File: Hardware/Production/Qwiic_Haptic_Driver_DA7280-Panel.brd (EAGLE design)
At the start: 123.2 x 117.3 mm, 758 parts, among them J1 QWIIC_RIGHT_ANGLE, J10 QWIIC_RIGHT_ANGLE, J13 QWIIC_RIGHT_ANGLE, J14 QWIIC_RIGHT_ANGLE, J17 QWIIC_RIGHT_ANGLE, J18 QWIIC_RIGHT_ANGLE, J2 QWIIC_RIGHT_ANGLE, J21 QWIIC_RIGHT_ANGLE, J22 QWIIC_RIGHT_ANGLE, J25 QWIIC_RIGHT_ANGLE, J26 QWIIC_RIGHT_ANGLE, J29 QWIIC_RIGHT_ANGLE, J30 QWIIC_RIGHT_ANGLE, J33 QWIIC_RIGHT_ANGLE, J34 QWIIC_RIGHT_ANGLE, J37 QWIIC_RIGHT_ANGLE, J38 QWIIC_RIGHT_ANGLE, J41 QWIIC_RIGHT_ANGLE, J42 QWIIC_RIGHT_ANGLE, J45 QWIIC_RIGHT_ANGLE, J46 QWIIC_RIGHT_ANGLE, J49 QWIIC_RIGHT_ANGLE, J5 QWIIC_RIGHT_ANGLE, J50 QWIIC_RIGHT_ANGLE, J53 QWIIC_RIGHT_ANGLE, J54 QWIIC_RIGHT_ANGLE, J57 QWIIC_RIGHT_ANGLE, J58 QWIIC_RIGHT_ANGLE, J6 QWIIC_RIGHT_ANGLE, J61 QWIIC_RIGHT_ANGLE, J62 QWIIC_RIGHT_ANGLE, J9 QWIIC_RIGHT_ANGLE, M1 G1040003D_LRA_CASTELLATED, M10 G1040003D_LRA_CASTELLATED, M11 G1040003D_LRA_CASTELLATED, M12 G1040003D_LRA_CASTELLATED, M13 G1040003D_LRA_CASTELLATED, M14 G1040003D_LRA_CASTELLATED, M15 G1040003D_LRA_CASTELLATED, M16 G1040003D_LRA_CASTELLATED, M2 G1040003D_LRA_CASTELLATED, M3 G1040003D_LRA_CASTELLATED, M4 G1040003D_LRA_CASTELLATED, M5 G1040003D_LRA_CASTELLATED, M6 G1040003D_LRA_CASTELLATED, M7 G1040003D_LRA_CASTELLATED, M8 G1040003D_LRA_CASTELLATED, M9 G1040003D_LRA_CASTELLATED, U1 HAPTIC_DRIVER_DA7280, U10 HAPTIC_DRIVER_DA7280, U11 HAPTIC_DRIVER_DA7280, U12 HAPTIC_DRIVER_DA7280, U13 HAPTIC_DRIVER_DA7280, U14 HAPTIC_DRIVER_DA7280, U15 HAPTIC_DRIVER_DA7280, U16 HAPTIC_DRIVER_DA7280, U2 HAPTIC_DRIVER_DA7280, U3 HAPTIC_DRIVER_DA7280, U4 HAPTIC_DRIVER_DA7280, U5 HAPTIC_DRIVER_DA7280, U6 HAPTIC_DRIVER_DA7280, U7 HAPTIC_DRIVER_DA7280, U8 HAPTIC_DRIVER_DA7280, U9 HAPTIC_DRIVER_DA7280

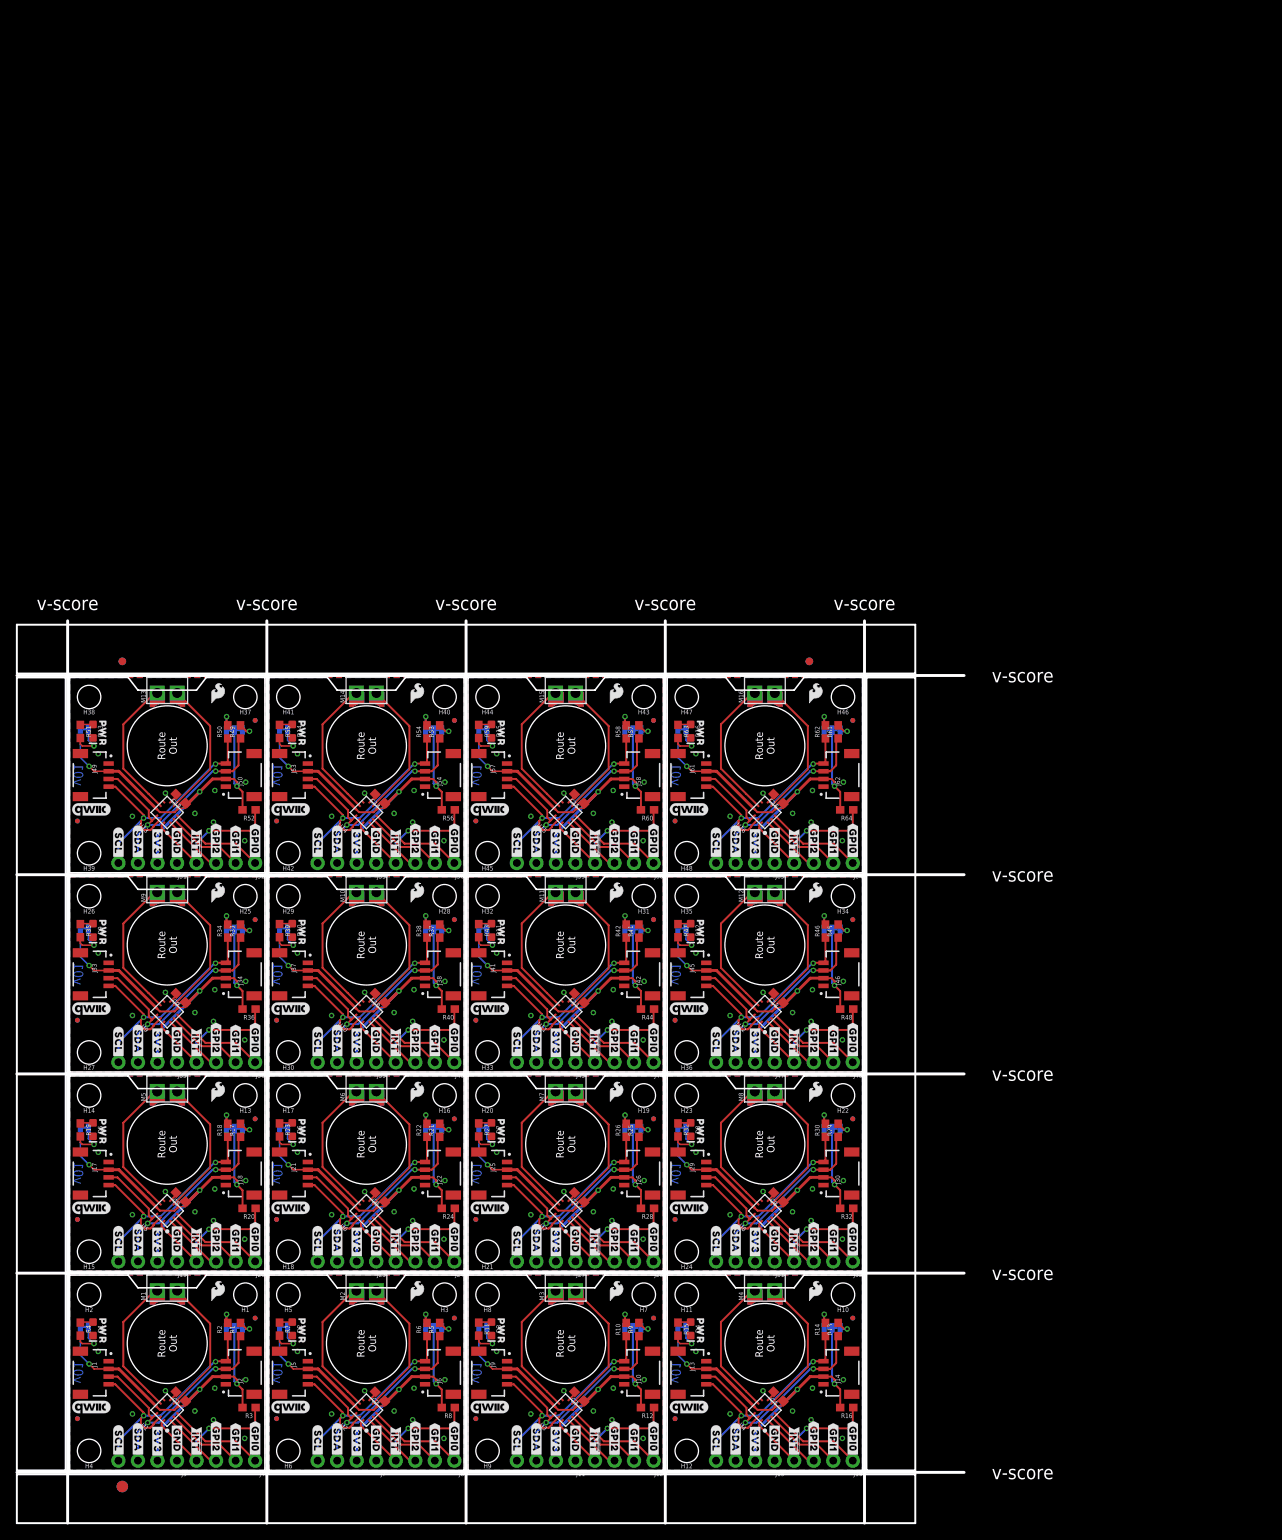
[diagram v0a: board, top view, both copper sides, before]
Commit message: Improves ground pour just a smidge, found better routing options when reviewing panel
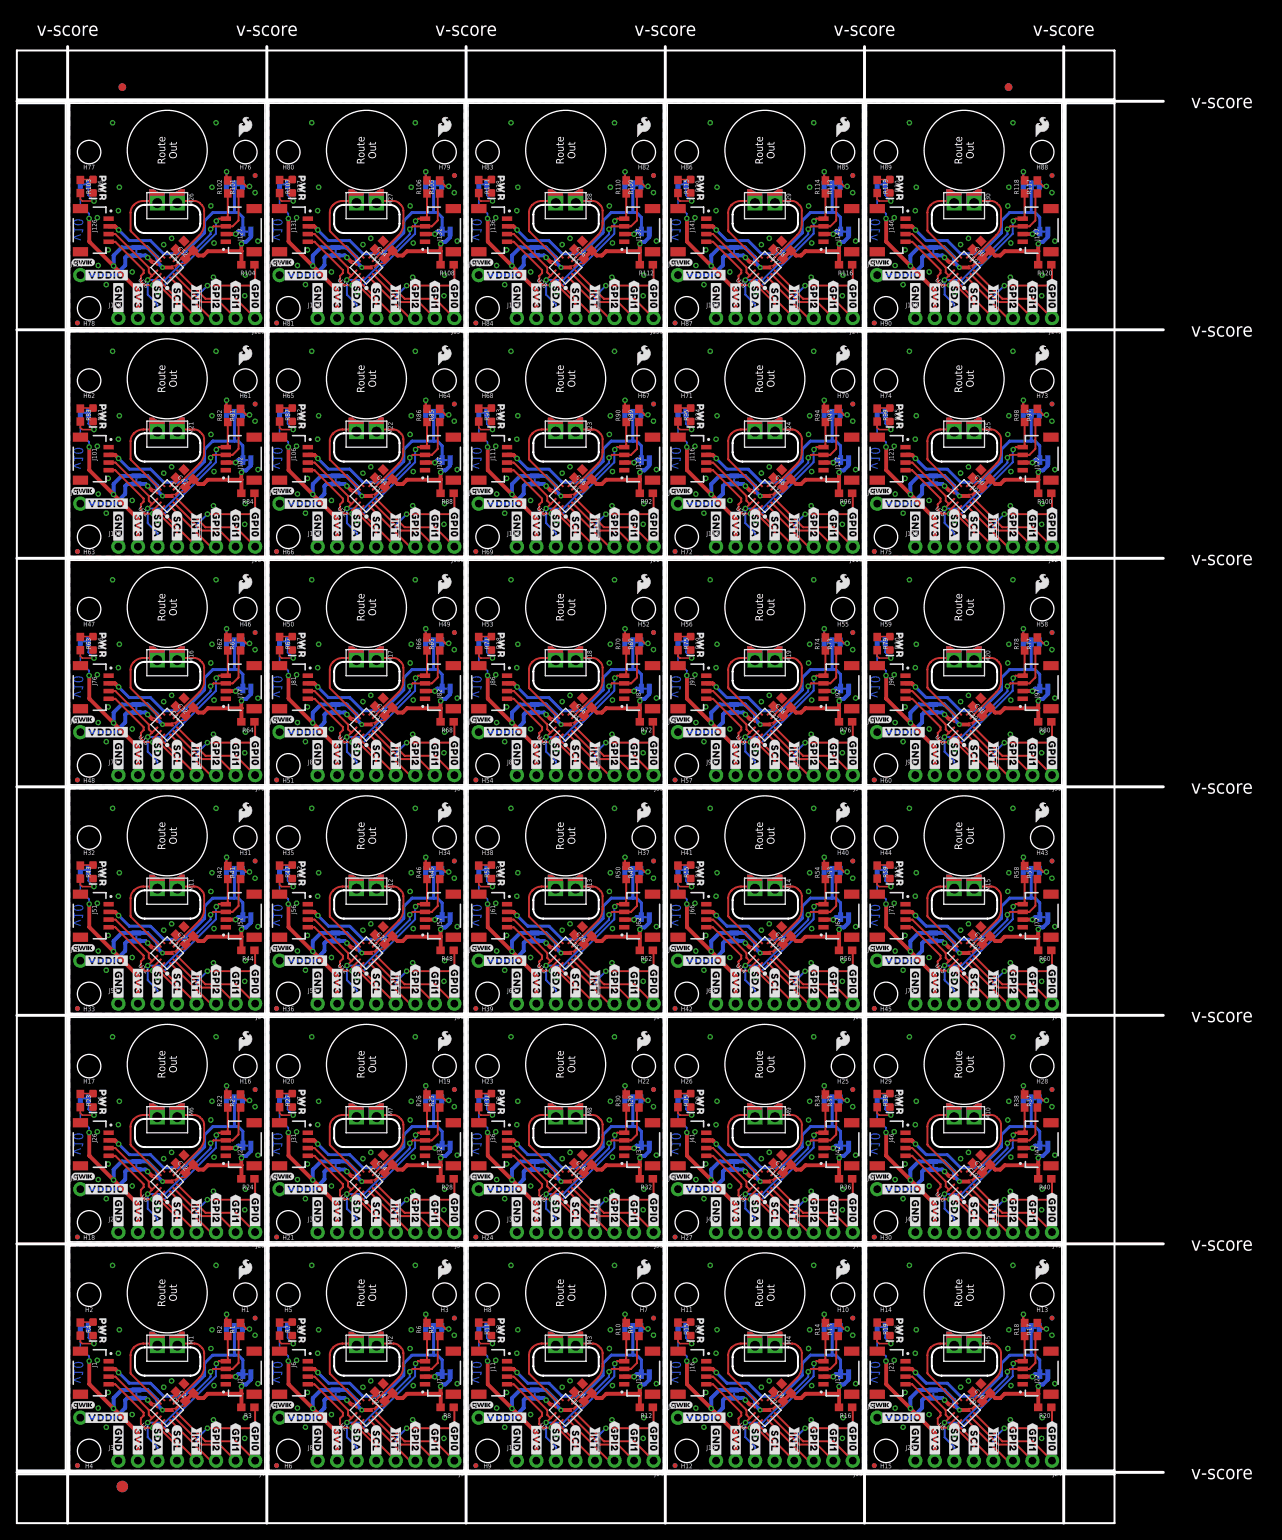
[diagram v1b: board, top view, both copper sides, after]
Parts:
- added C17, C19, C21, C23, C25, C27, C29, C31, C33, C35, C37, C39, C41, C43, C45, C47, C49, C51, C53, C55, C57, C59: 0.1uF, SparkFun-Capacitors:0603
- added C18, C20, C22, C24, C26, C28, C30, C32, C34, C36, C38, C40, C42, C44, C46, C48, C50, C52, C54, C56, C58, C60: 4.7uF, SparkFun-Capacitors:0603
- added D17, D18, D19, D20, D21, D22, D23, D24, D25, D26, D27, D28, D29, D30: RED, SparkFun-LED:LED-0603
- added FD100, FD101, FD102, FD103, FD104, FD105, FD106, FD107, FD108, FD109, FD110, FD111, FD112, FD113, FD114, FD115, FD116, FD117, FD118, FD119, FD120, FD65, FD66, FD67, FD68, FD69, FD70, FD71, FD72, FD73, FD74, FD75, FD76, FD77, FD78, FD79, FD80, FD81, FD82, FD83, FD84, FD85, FD86, FD87, FD88, FD89, FD90, FD91, FD92, FD93, FD94, FD95, FD96, FD97, FD98, FD99: FIDUCIALUFIDUCIAL, SparkFun-Aesthetics:FIDUCIAL-MICRO
- added H49, H50, H51, H52, H53, H54, H55, H56, H57, H58, H59, H60, H61, H62, H63, H64, H65, H66, H67, H68, H69, H70, H71, H72, H73, H74, H75, H76, H77, H78, H79, H80, H81, H82, H83, H84, H85, H86, H87, H88, H89, H90: STAND-OFFTIGHT, SparkFun-Hardware:STAND-OFF-TIGHT
- added J100, J105, J110, J115, J120, J125, J130, J135, J140, J145, J150, J65, J70, J75, J80, J85, J90, J95: (no value), SparkFun-Connectors:1X01_NO_SILK
- added J101, J102, J106, J107, J111, J112, J116, J117, J121, J122, J126, J127, J131, J132, J136, J137, J141, J142, J146, J147, J66, J67, J71, J72, J76, J77, J81, J82, J86, J87, J91, J92, J96, J97: QWIIC_RIGHT_ANGLE, SparkFun-Connectors:JST04_1MM_RA
- added J103, J104, J108, J109, J113, J114, J118, J119, J123, J124, J128, J129, J133, J134, J138, J139, J143, J144, J148, J149, J68, J69, J73, J74, J78, J79, J83, J84, J88, J89, J93, J94, J98, J99: (no value), SparkFun-Connectors:1X04_NO_SILK
- added JP100, JP101, JP103, JP104, JP105, JP107, JP108, JP109, JP111, JP112, JP113, JP115, JP116, JP117, JP119, JP120, JP33, JP35, JP36, JP37, JP39, JP40, JP41, JP43, JP44, JP45, JP47, JP48, JP49, JP51, JP52, JP53, JP55, JP56, JP57, JP59, JP60, JP61, JP63, JP64, JP65, JP67, JP68, JP69, JP71, JP72, JP73, JP75, JP76, JP77, JP79, JP80, JP81, JP83, JP84, JP85, JP87, JP88, JP89, JP91, JP92, JP93, JP95, JP96, JP97, JP99: LED, SparkFun-Jumpers:SMT-JUMPER_2_NC_TRACE_SILK
- added JP102, JP106, JP110, JP114, JP118, JP34, JP38, JP42, JP46, JP50, JP54, JP58, JP62, JP66, JP70, JP74, JP78, JP82, JP86, JP90, JP94, JP98: I2C_PU, SparkFun-Jumpers:SMT-JUMPER_3_2-NC_TRACE_SILK
- added LOGO1, LOGO11, LOGO13, LOGO15, LOGO17, LOGO19, LOGO2, LOGO21, LOGO23, LOGO25, LOGO27, LOGO29, LOGO31, LOGO33, LOGO35, LOGO37, LOGO39, LOGO41, LOGO43, LOGO45, LOGO47, LOGO49, LOGO5, LOGO51, LOGO53, LOGO55, LOGO57, LOGO59, LOGO7, LOGO9: OSHW-LOGOS, SparkFun-Aesthetics:OSHW-LOGO-S
- added LOGO10, LOGO12, LOGO14, LOGO16, LOGO18, LOGO20, LOGO22, LOGO24, LOGO26, LOGO28, LOGO3, LOGO30, LOGO32, LOGO34, LOGO36, LOGO38, LOGO4, LOGO40, LOGO42, LOGO44, LOGO46, LOGO48, LOGO50, LOGO52, LOGO54, LOGO56, LOGO58, LOGO6, LOGO60, LOGO8: SFE_LOGO_FLAME.1_INCH, SparkFun-Aesthetics:SFE_LOGO_FLAME_.1
- added M17, M18, M19, M20, M21, M22, M23, M24, M25, M26, M27, M28, M29, M30: G1040003D_LRA_CASTELLATED, TEMP:COIN_VIBRATION_MOTOR_CASTEL
- added R100, R104, R108, R112, R116, R120, R68, R72, R76, R80, R84, R88, R92, R96: 10k, SparkFun-Resistors:0603
- added R101, R102, R105, R106, R109, R110, R113, R114, R117, R118, R65, R66, R69, R70, R73, R74, R77, R78, R81, R82, R85, R86, R89, R90, R93, R94, R97, R98: 4.7k, SparkFun-Resistors:0603
- added R103, R107, R111, R115, R119, R67, R71, R75, R79, R83, R87, R91, R95, R99: 1k, SparkFun-Resistors:0603
- added U$417, U$437, U$446, U$466, U$475, U$495, U$504, U$524, U$533, U$553, U$562, U$582, U$591, U$611, U$620, U$640, U$649, U$669, U$678, U$698, U$707, U$727, U$736, U$756, U$765, U$785, U$794, U$814, U$823, U$843, U$852: (no value), top:#GND#0
- added U$418, U$447, U$476, U$505, U$534, U$563, U$592, U$621, U$650, U$679, U$708, U$737, U$766, U$795, U$824, U$853: (no value), top:#SCL#5
- added U$419, U$448, U$477, U$506, U$535, U$564, U$593, U$622, U$651, U$680, U$709, U$738, U$767, U$796, U$825, U$854: (no value), top:PWR72810
- added U$420, U$449, U$478, U$507, U$536, U$565, U$594, U$623, U$652, U$681, U$710, U$739, U$768, U$797, U$826, U$855: (no value), bot:#SCL#1
- added U$421, U$450, U$479, U$508, U$537, U$566, U$595, U$624, U$653, U$682, U$711, U$740, U$769, U$798, U$827, U$856: (no value), bot:#I2C#4
- added U$422, U$451, U$480, U$509, U$538, U$567, U$596, U$625, U$654, U$683, U$712, U$741, U$770, U$799, U$828, U$857: (no value), bot:#LED#4
- added U$423, U$452, U$481, U$510, U$539, U$568, U$597, U$626, U$655, U$684, U$713, U$742, U$771, U$800, U$829, U$858: (no value), top:#3V3#1
- added U$424, U$453, U$482, U$511, U$540, U$569, U$598, U$627, U$656, U$685, U$714, U$743, U$772, U$801, U$830, U$859: (no value), SparkFun-Aesthetics:SFE_LOGO_FLAME_.1
- added U$425, U$454, U$483, U$512, U$541, U$570, U$599, U$628, U$657, U$686, U$715, U$744, U$773, U$802, U$831, U$860: (no value), bot:##INT##3
- added U$426, U$455, U$484, U$513, U$542, U$571, U$600, U$629, U$658, U$687, U$716, U$745, U$774, U$803, U$832, U$861: (no value), top:##INT##6
- added U$427, U$456, U$485, U$514, U$543, U$572, U$601, U$630, U$659, U$688, U$717, U$746, U$775, U$804, U$833, U$862: (no value), top:#VDD#4
- added U$428, U$429, U$457, U$458, U$486, U$487, U$515, U$516, U$544, U$545, U$573, U$574, U$602, U$603, U$631, U$632, U$660, U$661, U$689, U$690, U$718, U$719, U$747, U$748, U$776, U$777, U$805, U$806, U$834, U$835, U$863, U$864: (no value), top:#VDDIO#5
- added U$430, U$459, U$488, U$517, U$546, U$575, U$604, U$633, U$662, U$691, U$720, U$749, U$778, U$807, U$836, U$865: (no value), top:HAPTIC6
- added U$431, U$460, U$489, U$518, U$547, U$576, U$605, U$634, U$663, U$692, U$721, U$750, U$779, U$808, U$837, U$866: (no value), top:MOTOR7
- added U$432, U$461, U$490, U$519, U$548, U$577, U$606, U$635, U$664, U$693, U$722, U$751, U$780, U$809, U$838, U$867: (no value), top:DRIVER8
- added U$433, U$462, U$491, U$520, U$549, U$578, U$607, U$636, U$665, U$694, U$723, U$752, U$781, U$810, U$839, U$868: (no value), top:DA72809
- added U$434, U$463, U$492, U$521, U$550, U$579, U$608, U$637, U$666, U$695, U$724, U$753, U$782, U$811, U$840, U$869: (no value), top:#IO#6
- added U$435, U$464, U$493, U$522, U$551, U$580, U$609, U$638, U$667, U$696, U$725, U$754, U$783, U$812, U$841, U$870: (no value), bot:#QISO#0
- added U$436, U$465, U$494, U$523, U$552, U$581, U$610, U$639, U$668, U$697, U$726, U$755, U$784, U$813, U$842: QWIIC_LOGO_3MM, SparkFun-Aesthetics:QWIIC_3MM
- added U$438, U$467, U$496, U$525, U$554, U$583, U$612, U$641, U$670, U$699, U$728, U$757, U$786, U$815, U$844: (no value), top:#GPI0#6
- added U$439, U$468, U$497, U$526, U$555, U$584, U$613, U$642, U$671, U$700, U$729, U$758, U$787, U$816, U$845: (no value), top:#GPI1#6
- added U$440, U$469, U$498, U$527, U$556, U$585, U$614, U$643, U$672, U$701, U$730, U$759, U$788, U$817, U$846: (no value), top:#GPI2#6
- added U$441, U$470, U$499, U$528, U$557, U$586, U$615, U$644, U$673, U$702, U$731, U$760, U$789, U$818, U$847: (no value), top:#SDA#4
- added U$442, U$471, U$500, U$529, U$558, U$587, U$616, U$645, U$674, U$703, U$732, U$761, U$790, U$819, U$848: (no value), bot:#GPI0#PWM#2
- added U$443, U$472, U$501, U$530, U$559, U$588, U$617, U$646, U$675, U$704, U$733, U$762, U$791, U$820, U$849: (no value), bot:#GPI1#2
- added U$444, U$473, U$502, U$531, U$560, U$589, U$618, U$647, U$676, U$705, U$734, U$763, U$792, U$821, U$850: (no value), bot:#GPI2#2
- added U$445, U$474, U$503, U$532, U$561, U$590, U$619, U$648, U$677, U$706, U$735, U$764, U$793, U$822, U$851: (no value), bot:#SDA#0
- added U17, U18, U19, U20, U21, U22, U23, U24, U25, U26, U27, U28, U29, U30: HAPTIC_DRIVER_DA7280, TEMP:QFN_DA7280
- C10, C12, C14, C16, C2, C4, C6, C8: value 0.1uF -> 4.7uF
- J10, J25, J30, J45, J5, J50: value QWIIC_RIGHT_ANGLE -> (none); device SparkFun-Connectors:JST04_1MM_RA -> SparkFun-Connectors:1X01_NO_SILK
- J11, J12, J16, J27, J31, J32, J36, J47, J51, J52, J56, J7: value (none) -> QWIIC_RIGHT_ANGLE; device SparkFun-Connectors:1X04_NO_SILK -> SparkFun-Connectors:JST04_1MM_RA
- J13, J14, J18, J29, J33, J34, J38, J49, J53, J54, J58, J9: value QWIIC_RIGHT_ANGLE -> (none); device SparkFun-Connectors:JST04_1MM_RA -> SparkFun-Connectors:1X04_NO_SILK
- J15, J20, J35, J40, J55, J60: device SparkFun-Connectors:1X04_NO_SILK -> SparkFun-Connectors:1X01_NO_SILK
- JP12, JP16, JP20, JP24, JP28, JP32, JP4, JP8: value I2C_PU -> LED; device SparkFun-Jumpers:SMT-JUMPER_3_2-NC_TRACE_SILK -> SparkFun-Jumpers:SMT-JUMPER_2_NC_TRACE_SILK
- U$1: value QWIIC_LOGO_5MM -> QWIIC_LOGO_3MM; device SparkFun-Aesthetics:QWIIC_5MM -> SparkFun-Aesthetics:QWIIC_3MM
- U$10, U$112: device top:HAPTIC7 -> top:MOTOR7
- U$100: device top:#3V3#1 -> top:PWR72810
- U$101, U$362: device SparkFun-Aesthetics:SFE_LOGO_FLAME_.1 -> bot:#SCL#1
- U$102: device SparkFun-Aesthetics:SFE_LOGO_FLAME_.1 -> bot:#I2C#4
- U$103: device bot:##INT##3 -> bot:#LED#4
- U$104: device top:##INT##6 -> top:#3V3#1
- U$105: value QWIIC_LOGO_5MM -> (none); device SparkFun-Aesthetics:QWIIC_5MM -> SparkFun-Aesthetics:SFE_LOGO_FLAME_.1
- U$106, U$222: device top:#GND#0 -> bot:##INT##3
- U$107: device top:#GPI0#6 -> top:##INT##6
- U$108: device top:#GPI1#6 -> top:#VDD#4
- U$109: device top:#GPI2#6 -> top:#VDDIO#5
- U$11, U$113: device top:MOTOR_DRIVER8 -> top:DRIVER8
- U$110, U$370: device top:#SDA#4 -> top:#VDDIO#5
- U$111, U$9: device top:DA72809 -> top:HAPTIC6
- U$114: device bot:#GPI0#PWM#2 -> top:DA72809
- U$115: device bot:#GPI1#2 -> top:#IO#6
- U$116: device bot:#GPI2#2 -> bot:#QISO#0
- U$117: value (none) -> QWIIC_LOGO_3MM; device bot:#SDA#0 -> SparkFun-Aesthetics:QWIIC_3MM
- U$119: device top:#SCL#5 -> top:#GPI0#6
- U$120: device top:PWR72810 -> top:#GPI1#6
- U$121: device bot:#SCL#1 -> top:#GPI2#6
- U$122: device SparkFun-Aesthetics:OSHW-LOGO-MINI -> top:#SDA#4
- U$123: device bot:#I2C#4 -> bot:#GPI0#PWM#2
- U$124: device bot:#LED#4 -> bot:#GPI1#2
- U$125, U$386: device top:#3V3#1 -> bot:#GPI2#2
- U$126: device top:#3V3#1 -> bot:#SDA#0
- U$127, U$205, U$388: device SparkFun-Aesthetics:SFE_LOGO_FLAME_.1 -> top:#GND#0
- U$128: device SparkFun-Aesthetics:SFE_LOGO_FLAME_.1 -> top:#SCL#5
- U$129: device bot:##INT##3 -> top:PWR72810
- U$130: device top:##INT##6 -> bot:#SCL#1
- U$131: value QWIIC_LOGO_5MM -> (none); device SparkFun-Aesthetics:QWIIC_5MM -> bot:#I2C#4
- U$132, U$248: device top:#GND#0 -> bot:#LED#4
- U$133: device top:#GPI0#6 -> top:#3V3#1
- U$134: device top:#GPI1#6 -> SparkFun-Aesthetics:SFE_LOGO_FLAME_.1
- U$135: device top:#GPI2#6 -> bot:##INT##3
- U$136: device top:#SDA#4 -> top:##INT##6
- U$137: device top:DA72809 -> top:#VDD#4
- U$138: device top:HAPTIC7 -> top:#VDDIO#5
- U$139, U$399: device top:MOTOR_DRIVER8 -> top:#VDDIO#5
- U$140: device bot:#GPI0#PWM#2 -> top:HAPTIC6
- U$141: device bot:#GPI1#2 -> top:MOTOR7
- U$142: device bot:#GPI2#2 -> top:DRIVER8
- U$143: device bot:#SDA#0 -> top:DA72809
- U$144: device top:#GND#0 -> top:#IO#6
- U$145: device top:#SCL#5 -> bot:#QISO#0
- U$146: value (none) -> QWIIC_LOGO_3MM; device top:PWR72810 -> SparkFun-Aesthetics:QWIIC_3MM
- U$147, U$69: device bot:#SCL#1 -> top:#GND#0
- U$148: device SparkFun-Aesthetics:OSHW-LOGO-MINI -> top:#GPI0#6
- U$149: device bot:#I2C#4 -> top:#GPI1#6
- U$15, U$196, U$80: device top:#GND#0 -> top:#VDDIO#5
- U$150: device bot:#LED#4 -> top:#GPI2#6
- U$151, U$412: device top:#3V3#1 -> top:#SDA#4
- U$152: device top:#3V3#1 -> bot:#GPI0#PWM#2
- U$153, U$414: device SparkFun-Aesthetics:SFE_LOGO_FLAME_.1 -> bot:#GPI1#2
- U$154: device SparkFun-Aesthetics:SFE_LOGO_FLAME_.1 -> bot:#GPI2#2
- U$155: device bot:##INT##3 -> bot:#SDA#0
- U$156, U$234: device top:##INT##6 -> top:#GND#0
- U$157: value QWIIC_LOGO_5MM -> (none); device SparkFun-Aesthetics:QWIIC_5MM -> top:#SCL#5
- U$158, U$274: device top:#GND#0 -> top:PWR72810
- U$159: device top:#GPI0#6 -> bot:#SCL#1
- U$160: device top:#GPI1#6 -> bot:#I2C#4
- U$161: device top:#GPI2#6 -> bot:#LED#4
- U$162: device top:#SDA#4 -> top:#3V3#1
- U$163: device top:DA72809 -> SparkFun-Aesthetics:SFE_LOGO_FLAME_.1
- U$164: device top:HAPTIC7 -> bot:##INT##3
- U$165: device top:MOTOR_DRIVER8 -> top:##INT##6
- U$166: device bot:#GPI0#PWM#2 -> top:#VDD#4
- U$167: device bot:#GPI1#2 -> top:#VDDIO#5
- U$168: device bot:#GPI2#2 -> top:#VDDIO#5
- U$169: device bot:#SDA#0 -> top:HAPTIC6
- U$17: value (none) -> QWIIC_LOGO_3MM; device SparkFun-Aesthetics:SFE_LOGO_FLAME_.1 -> SparkFun-Aesthetics:QWIIC_3MM
- U$170, U$54: device top:#GND#0 -> top:MOTOR7
- U$171: device top:#SCL#5 -> top:DRIVER8
- U$172: device top:PWR72810 -> top:DA72809
- U$173: device bot:#SCL#1 -> top:#IO#6
- U$174: device SparkFun-Aesthetics:OSHW-LOGO-MINI -> bot:#QISO#0
- U$175: value (none) -> QWIIC_LOGO_3MM; device bot:#I2C#4 -> SparkFun-Aesthetics:QWIIC_3MM
- U$176, U$98: device bot:#LED#4 -> top:#GND#0
- U$177: device top:#3V3#1 -> top:#GPI0#6
- U$178: device top:#3V3#1 -> top:#GPI1#6
- U$179: device SparkFun-Aesthetics:SFE_LOGO_FLAME_.1 -> top:#GPI2#6
- U$180: device SparkFun-Aesthetics:SFE_LOGO_FLAME_.1 -> top:#SDA#4
- U$181: device bot:##INT##3 -> bot:#GPI0#PWM#2
- U$182: device top:##INT##6 -> bot:#GPI1#2
- U$183: value QWIIC_LOGO_5MM -> (none); device SparkFun-Aesthetics:QWIIC_5MM -> bot:#GPI2#2
- U$184, U$300: device top:#GND#0 -> bot:#SDA#0
- U$185, U$263: device top:#GPI0#6 -> top:#GND#0
- U$186: device top:#GPI1#6 -> top:#SCL#5
- U$187: device top:#GPI2#6 -> top:PWR72810
- U$188: device top:#SDA#4 -> bot:#SCL#1
- U$189: device top:DA72809 -> bot:#I2C#4
- U$190: device top:HAPTIC7 -> bot:#LED#4
- U$191: device top:MOTOR_DRIVER8 -> top:#3V3#1
- U$192: device bot:#GPI0#PWM#2 -> SparkFun-Aesthetics:SFE_LOGO_FLAME_.1
- U$193: device bot:#GPI1#2 -> bot:##INT##3
- U$194: device bot:#GPI2#2 -> top:##INT##6
- U$195: device bot:#SDA#0 -> top:#VDD#4
- U$197: device top:#SCL#5 -> top:#VDDIO#5
- U$198: device top:PWR72810 -> top:HAPTIC6
- U$199: device bot:#SCL#1 -> top:MOTOR7
- U$200: device SparkFun-Aesthetics:OSHW-LOGO-MINI -> top:DRIVER8
- U$201: device bot:#I2C#4 -> top:DA72809
- U$202: device bot:#LED#4 -> top:#IO#6
- U$203: device top:#3V3#1 -> bot:#QISO#0
- U$204: value (none) -> QWIIC_LOGO_3MM; device top:#3V3#1 -> SparkFun-Aesthetics:QWIIC_3MM
- U$206: device SparkFun-Aesthetics:SFE_LOGO_FLAME_.1 -> top:#GPI0#6
- U$207: device bot:##INT##3 -> top:#GPI1#6
- U$208: device top:##INT##6 -> top:#GPI2#6
- U$209: value QWIIC_LOGO_5MM -> (none); device SparkFun-Aesthetics:QWIIC_5MM -> top:#SDA#4
- U$210, U$326: device top:#GND#0 -> bot:#GPI0#PWM#2
- U$211: device top:#GPI0#6 -> bot:#GPI1#2
- U$212: device top:#GPI1#6 -> bot:#GPI2#2
- U$213: device top:#GPI2#6 -> bot:#SDA#0
- U$214, U$292: device top:#SDA#4 -> top:#GND#0
- U$215: device top:DA72809 -> top:#SCL#5
- U$216: device top:HAPTIC7 -> top:PWR72810
- U$217: device top:MOTOR_DRIVER8 -> bot:#SCL#1
- U$218: device bot:#GPI0#PWM#2 -> bot:#I2C#4
- U$219: device bot:#GPI1#2 -> bot:#LED#4
- U$22, U$330, U$408: device SparkFun-Aesthetics:OSHW-LOGO-MINI -> top:#GND#0
- U$220: device bot:#GPI2#2 -> top:#3V3#1
- U$221: device bot:#SDA#0 -> SparkFun-Aesthetics:SFE_LOGO_FLAME_.1
- U$223: device top:#SCL#5 -> top:##INT##6
- U$224: device top:PWR72810 -> top:#VDD#4
- U$225: device bot:#SCL#1 -> top:#VDDIO#5
- U$226: device SparkFun-Aesthetics:OSHW-LOGO-MINI -> top:#VDDIO#5
- U$227: device bot:#I2C#4 -> top:HAPTIC6
- U$228: device bot:#LED#4 -> top:MOTOR7
- U$229: device top:#3V3#1 -> top:DRIVER8
- U$230: device top:#3V3#1 -> top:DA72809
- U$231: device SparkFun-Aesthetics:SFE_LOGO_FLAME_.1 -> top:#IO#6
- U$232: device SparkFun-Aesthetics:SFE_LOGO_FLAME_.1 -> bot:#QISO#0
- U$233: value (none) -> QWIIC_LOGO_3MM; device bot:##INT##3 -> SparkFun-Aesthetics:QWIIC_3MM
- U$235: value QWIIC_LOGO_5MM -> (none); device SparkFun-Aesthetics:QWIIC_5MM -> top:#GPI0#6
- U$236, U$352: device top:#GND#0 -> top:#GPI1#6
- U$237: device top:#GPI0#6 -> top:#GPI2#6
- U$238: device top:#GPI1#6 -> top:#SDA#4
- U$239: device top:#GPI2#6 -> bot:#GPI0#PWM#2
- U$240: device top:#SDA#4 -> bot:#GPI1#2
- U$241: device top:DA72809 -> bot:#GPI2#2
- U$242: device top:HAPTIC7 -> bot:#SDA#0
- U$243, U$321: device top:MOTOR_DRIVER8 -> top:#GND#0
- U$244: device bot:#GPI0#PWM#2 -> top:#SCL#5
- U$245: device bot:#GPI1#2 -> top:PWR72810
- U$246: device bot:#GPI2#2 -> bot:#SCL#1
- U$247: device bot:#SDA#0 -> bot:#I2C#4
- U$249: device top:#SCL#5 -> top:#3V3#1
- U$25, U$255: device top:#3V3#1 -> top:#VDDIO#5
- U$250: device top:PWR72810 -> SparkFun-Aesthetics:SFE_LOGO_FLAME_.1
- U$251: device bot:#SCL#1 -> bot:##INT##3
- U$252: device SparkFun-Aesthetics:OSHW-LOGO-MINI -> top:##INT##6
- U$253: device bot:#I2C#4 -> top:#VDD#4
- U$254: device bot:#LED#4 -> top:#VDDIO#5
- U$256: device top:#3V3#1 -> top:HAPTIC6
- U$257: device SparkFun-Aesthetics:SFE_LOGO_FLAME_.1 -> top:MOTOR7
- U$258: device SparkFun-Aesthetics:SFE_LOGO_FLAME_.1 -> top:DRIVER8
- U$259: device bot:##INT##3 -> top:DA72809
- U$260: device top:##INT##6 -> top:#IO#6
- U$261: value QWIIC_LOGO_5MM -> (none); device SparkFun-Aesthetics:QWIIC_5MM -> bot:#QISO#0
- U$262, U$378: value (none) -> QWIIC_LOGO_3MM; device top:#GND#0 -> SparkFun-Aesthetics:QWIIC_3MM
- U$264: device top:#GPI1#6 -> top:#GPI0#6
- U$265: device top:#GPI2#6 -> top:#GPI1#6
- U$266: device top:#SDA#4 -> top:#GPI2#6
- U$267: device top:DA72809 -> top:#SDA#4
- U$268: device top:HAPTIC7 -> bot:#GPI0#PWM#2
- U$269: device top:MOTOR_DRIVER8 -> bot:#GPI1#2
- U$270: device bot:#GPI0#PWM#2 -> bot:#GPI2#2
- U$271: device bot:#GPI1#2 -> bot:#SDA#0
- U$272, U$350: device bot:#GPI2#2 -> top:#GND#0
- U$273: device bot:#SDA#0 -> top:#SCL#5
- U$275: device top:#SCL#5 -> bot:#SCL#1
- U$276: device top:PWR72810 -> bot:#I2C#4
- U$277: device bot:#SCL#1 -> bot:#LED#4
- U$278: device SparkFun-Aesthetics:OSHW-LOGO-MINI -> top:#3V3#1
- U$279: device bot:#I2C#4 -> SparkFun-Aesthetics:SFE_LOGO_FLAME_.1
- U$280: device bot:#LED#4 -> bot:##INT##3
- U$281: device top:#3V3#1 -> top:##INT##6
- U$282: device top:#3V3#1 -> top:#VDD#4
- U$283, U$284: device SparkFun-Aesthetics:SFE_LOGO_FLAME_.1 -> top:#VDDIO#5
- U$285: device bot:##INT##3 -> top:HAPTIC6
- U$286: device top:##INT##6 -> top:MOTOR7
- U$287: value QWIIC_LOGO_5MM -> (none); device SparkFun-Aesthetics:QWIIC_5MM -> top:DRIVER8
- U$288, U$404: device top:#GND#0 -> top:DA72809
- U$289: device top:#GPI0#6 -> top:#IO#6
- U$29: device top:#GPI0#6 -> top:DA72809
- U$290: device top:#GPI1#6 -> bot:#QISO#0
- U$291: value (none) -> QWIIC_LOGO_3MM; device top:#GPI2#6 -> SparkFun-Aesthetics:QWIIC_3MM
- U$293: device top:DA72809 -> top:#GPI0#6
- U$294: device top:HAPTIC7 -> top:#GPI1#6
- U$295: device top:MOTOR_DRIVER8 -> top:#GPI2#6
- U$296: device bot:#GPI0#PWM#2 -> top:#SDA#4
- U$297: device bot:#GPI1#2 -> bot:#GPI0#PWM#2
- U$298: device bot:#GPI2#2 -> bot:#GPI1#2
- U$299: device bot:#SDA#0 -> bot:#GPI2#2
- U$30: device top:#GPI1#6 -> top:#IO#6
- U$301, U$379: device top:#SCL#5 -> top:#GND#0
- U$302: device top:PWR72810 -> top:#SCL#5
- U$303: device bot:#SCL#1 -> top:PWR72810
- U$304: device SparkFun-Aesthetics:OSHW-LOGO-MINI -> bot:#SCL#1
- U$308, U$47: device top:#3V3#1 -> SparkFun-Aesthetics:SFE_LOGO_FLAME_.1
- U$309: device SparkFun-Aesthetics:SFE_LOGO_FLAME_.1 -> bot:##INT##3
- U$31: device top:#GPI2#6 -> bot:#QISO#0
- U$310, U$49: device SparkFun-Aesthetics:SFE_LOGO_FLAME_.1 -> top:##INT##6
- U$311: device bot:##INT##3 -> top:#VDD#4
- U$312, U$52: device top:##INT##6 -> top:#VDDIO#5
- U$313: value QWIIC_LOGO_5MM -> (none); device SparkFun-Aesthetics:QWIIC_5MM -> top:#VDDIO#5
- U$314: device top:#GND#0 -> top:HAPTIC6
- U$315: device top:#GPI0#6 -> top:MOTOR7
- U$316: device top:#GPI1#6 -> top:DRIVER8
- U$317: device top:#GPI2#6 -> top:DA72809
- U$318: device top:#SDA#4 -> top:#IO#6
- U$319: device top:DA72809 -> bot:#QISO#0
- U$32: device top:#SDA#4 -> top:#GPI0#6
- U$320: value (none) -> QWIIC_LOGO_3MM; device top:HAPTIC7 -> SparkFun-Aesthetics:QWIIC_3MM
- U$322: device bot:#GPI0#PWM#2 -> top:#GPI0#6
- U$323: device bot:#GPI1#2 -> top:#GPI1#6
- U$324: device bot:#GPI2#2 -> top:#GPI2#6
- U$325: device bot:#SDA#0 -> top:#SDA#4
- U$327: device top:#SCL#5 -> bot:#GPI1#2
- U$328: device top:PWR72810 -> bot:#GPI2#2
- U$329: device bot:#SCL#1 -> bot:#SDA#0
- U$33: device top:DA72809 -> top:#GPI1#6
- U$331: device bot:#I2C#4 -> top:#SCL#5
- U$332: device bot:#LED#4 -> top:PWR72810
- U$333: device top:#3V3#1 -> bot:#SCL#1
- U$334, U$73: device top:#3V3#1 -> bot:#I2C#4
- U$335: device SparkFun-Aesthetics:SFE_LOGO_FLAME_.1 -> bot:#LED#4
- U$336, U$75: device SparkFun-Aesthetics:SFE_LOGO_FLAME_.1 -> top:#3V3#1
- U$337: device bot:##INT##3 -> SparkFun-Aesthetics:SFE_LOGO_FLAME_.1
- U$338: device top:##INT##6 -> bot:##INT##3
- U$339: value QWIIC_LOGO_5MM -> (none); device SparkFun-Aesthetics:QWIIC_5MM -> top:##INT##6
- U$34: device top:HAPTIC7 -> top:#GPI2#6
- U$340: device top:#GND#0 -> top:#VDD#4
- U$341, U$81: device top:#GPI0#6 -> top:#VDDIO#5
- U$342: device top:#GPI1#6 -> top:#VDDIO#5
- U$343: device top:#GPI2#6 -> top:HAPTIC6
- U$344: device top:#SDA#4 -> top:MOTOR7
- U$345: device top:DA72809 -> top:DRIVER8
- U$346: device top:HAPTIC7 -> top:DA72809
- U$347: device top:MOTOR_DRIVER8 -> top:#IO#6
- U$348: device bot:#GPI0#PWM#2 -> bot:#QISO#0
- U$349: value (none) -> QWIIC_LOGO_3MM; device bot:#GPI1#2 -> SparkFun-Aesthetics:QWIIC_3MM
- U$35: device top:MOTOR_DRIVER8 -> top:#SDA#4
- U$351: device bot:#SDA#0 -> top:#GPI0#6
- U$353: device top:#SCL#5 -> top:#GPI2#6
- U$354: device top:PWR72810 -> top:#SDA#4
- U$355: device bot:#SCL#1 -> bot:#GPI0#PWM#2
- U$356: device SparkFun-Aesthetics:OSHW-LOGO-MINI -> bot:#GPI1#2
- U$357: device bot:#I2C#4 -> bot:#GPI2#2
- U$358: device bot:#LED#4 -> bot:#SDA#0
- U$359: device top:#3V3#1 -> top:#GND#0
- U$360, U$99: device top:#3V3#1 -> top:#SCL#5
- U$361: device SparkFun-Aesthetics:SFE_LOGO_FLAME_.1 -> top:PWR72810
- U$363: device bot:##INT##3 -> bot:#I2C#4
- U$364: device top:##INT##6 -> bot:#LED#4
- U$365: value QWIIC_LOGO_5MM -> (none); device SparkFun-Aesthetics:QWIIC_5MM -> top:#3V3#1
- U$366: device top:#GND#0 -> SparkFun-Aesthetics:SFE_LOGO_FLAME_.1
- U$367: device top:#GPI0#6 -> bot:##INT##3
- U$368: device top:#GPI1#6 -> top:##INT##6
- U$369: device top:#GPI2#6 -> top:#VDD#4
- U$371: device top:DA72809 -> top:#VDDIO#5
- U$372: device top:HAPTIC7 -> top:HAPTIC6
- U$373: device top:MOTOR_DRIVER8 -> top:MOTOR7
- U$374: device bot:#GPI0#PWM#2 -> top:DRIVER8
- U$375: device bot:#GPI1#2 -> top:DA72809
- U$376: device bot:#GPI2#2 -> top:#IO#6
- U$377: device bot:#SDA#0 -> bot:#QISO#0
- U$380: device top:PWR72810 -> top:#GPI0#6
- U$381: device bot:#SCL#1 -> top:#GPI1#6
- U$382: device SparkFun-Aesthetics:OSHW-LOGO-MINI -> top:#GPI2#6
- U$383: device bot:#I2C#4 -> top:#SDA#4
- U$384: device bot:#LED#4 -> bot:#GPI0#PWM#2
- U$385: device top:#3V3#1 -> bot:#GPI1#2
- U$387: device SparkFun-Aesthetics:SFE_LOGO_FLAME_.1 -> bot:#SDA#0
- U$389: device bot:##INT##3 -> top:#SCL#5
- U$390: device top:##INT##6 -> top:PWR72810
- U$391: value QWIIC_LOGO_5MM -> (none); device SparkFun-Aesthetics:QWIIC_5MM -> bot:#SCL#1
- U$392: device top:#GND#0 -> bot:#I2C#4
- U$393: device top:#GPI0#6 -> bot:#LED#4
- U$394: device top:#GPI1#6 -> top:#3V3#1
- U$395: device top:#GPI2#6 -> SparkFun-Aesthetics:SFE_LOGO_FLAME_.1
- U$396: device top:#SDA#4 -> bot:##INT##3
- U$397: device top:DA72809 -> top:##INT##6
- U$398: device top:HAPTIC7 -> top:#VDD#4
- U$400: device bot:#GPI0#PWM#2 -> top:#VDDIO#5
- U$401: device bot:#GPI1#2 -> top:HAPTIC6
- U$402: device bot:#GPI2#2 -> top:MOTOR7
- U$403: device bot:#SDA#0 -> top:DRIVER8
- U$405: device top:#SCL#5 -> top:#IO#6
- U$406: device top:PWR72810 -> bot:#QISO#0
- U$407: value (none) -> QWIIC_LOGO_3MM; device bot:#SCL#1 -> SparkFun-Aesthetics:QWIIC_3MM
- U$409: device bot:#I2C#4 -> top:#GPI0#6
- U$410: device bot:#LED#4 -> top:#GPI1#6
- U$411: device top:#3V3#1 -> top:#GPI2#6
- U$413: device SparkFun-Aesthetics:SFE_LOGO_FLAME_.1 -> bot:#GPI0#PWM#2
- U$415: device bot:##INT##3 -> bot:#GPI2#2
- U$416: device top:##INT##6 -> bot:#SDA#0
- U$44: device SparkFun-Aesthetics:OSHW-LOGO-MINI -> bot:#I2C#4
- U$45: device bot:#I2C#4 -> bot:#LED#4
- U$46: device bot:#LED#4 -> top:#3V3#1
- U$48: device top:#3V3#1 -> bot:##INT##3
- U$50: device SparkFun-Aesthetics:SFE_LOGO_FLAME_.1 -> top:#VDD#4
- U$51: device bot:##INT##3 -> top:#VDDIO#5
- U$53: value QWIIC_LOGO_5MM -> (none); device SparkFun-Aesthetics:QWIIC_5MM -> top:HAPTIC6
- U$55: device top:#GPI0#6 -> top:DRIVER8
- U$56: device top:#GPI1#6 -> top:DA72809
- U$57: device top:#GPI2#6 -> top:#IO#6
- U$58: device top:#SDA#4 -> bot:#QISO#0
- U$59: value (none) -> QWIIC_LOGO_3MM; device top:DA72809 -> SparkFun-Aesthetics:QWIIC_3MM
- U$60: device top:HAPTIC7 -> top:#GND#0
- U$61: device top:MOTOR_DRIVER8 -> top:#GPI0#6
- U$62: device bot:#GPI0#PWM#2 -> top:#GPI1#6
- U$63: device bot:#GPI1#2 -> top:#GPI2#6
- U$64: device bot:#GPI2#2 -> top:#SDA#4
- U$65: device bot:#SDA#0 -> bot:#GPI0#PWM#2
- U$66: device top:#GND#0 -> bot:#GPI1#2
- U$67: device top:#SCL#5 -> bot:#GPI2#2
- U$68: device top:PWR72810 -> bot:#SDA#0
- U$7, U$79: value QWIIC_LOGO_5MM -> (none); device SparkFun-Aesthetics:QWIIC_5MM -> top:#VDD#4
- U$70: device SparkFun-Aesthetics:OSHW-LOGO-MINI -> top:#SCL#5
- U$71: device bot:#I2C#4 -> top:PWR72810
- U$72: device bot:#LED#4 -> bot:#SCL#1
- U$74: device top:#3V3#1 -> bot:#LED#4
- U$82: device top:#GPI1#6 -> top:HAPTIC6
- U$83: device top:#GPI2#6 -> top:MOTOR7
- U$84: device top:#SDA#4 -> top:DRIVER8
- U$86: device top:HAPTIC7 -> top:#IO#6
- U$87: device top:MOTOR_DRIVER8 -> bot:#QISO#0
- U$88: value (none) -> QWIIC_LOGO_3MM; device bot:#GPI0#PWM#2 -> SparkFun-Aesthetics:QWIIC_3MM
- U$89: device bot:#GPI1#2 -> top:#GND#0
- U$90: device bot:#GPI2#2 -> top:#GPI0#6
- U$91: device bot:#SDA#0 -> top:#GPI1#6
- U$92: device top:#GND#0 -> top:#GPI2#6
- U$93: device top:#SCL#5 -> top:#SDA#4
- U$94: device top:PWR72810 -> bot:#GPI0#PWM#2
- U$95: device bot:#SCL#1 -> bot:#GPI1#2
- U$96: device SparkFun-Aesthetics:OSHW-LOGO-MINI -> bot:#GPI2#2
- U$97: device bot:#I2C#4 -> bot:#SDA#0
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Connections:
- removed net 3.3V: C1.1, J1.2, J2.2, J3.2, JP1.2, JP3.2, R3.2, U1.P4, U1.P9
- removed net 3.3V1: C2.1, J5.2, J6.2, J7.2, JP2.2, JP4.2, R8.2, U2.P4, U2.P9
- removed net 3.3V10: C11.1, J41.2, J42.2, J43.2, JP21.2, JP22.2, R44.2, U11.P4, U11.P9
- removed net 3.3V11: C12.1, J45.2, J46.2, J47.2, JP23.2, JP24.2, R48.2, U12.P4, U12.P9
- removed net 3.3V12: C13.1, J49.2, J50.2, J51.2, JP25.2, JP26.2, R52.2, U13.P4, U13.P9
- removed net 3.3V13: C14.1, J53.2, J54.2, J55.2, JP27.2, JP28.2, R56.2, U14.P4, U14.P9
- removed net 3.3V14: C15.1, J57.2, J58.2, J59.2, JP29.2, JP30.2, R60.2, U15.P4, U15.P9
- removed net 3.3V15: C16.1, J61.2, J62.2, J63.2, JP31.2, JP32.2, R64.2, U16.P4, U16.P9
- removed net 3.3V2: C3.1, J10.2, J11.2, J9.2, JP5.2, JP6.2, R12.2, U3.P4, U3.P9
- removed net 3.3V3: C4.1, J13.2, J14.2, J15.2, JP7.2, JP8.2, R16.2, U4.P4, U4.P9
- removed net 3.3V4: C5.1, J17.2, J18.2, J19.2, JP10.2, JP9.2, R20.2, U5.P4, U5.P9
- removed net 3.3V5: C6.1, J21.2, J22.2, J23.2, JP11.2, JP12.2, R24.2, U6.P4, U6.P9
- removed net 3.3V6: C7.1, J25.2, J26.2, J27.2, JP13.2, JP14.2, R28.2, U7.P4, U7.P9
- removed net 3.3V7: C8.1, J29.2, J30.2, J31.2, JP15.2, JP16.2, R32.2, U8.P4, U8.P9
- removed net 3.3V8: C9.1, J33.2, J34.2, J35.2, JP17.2, JP18.2, R36.2, U9.P4, U9.P9
- removed net 3.3V9: C10.1, J37.2, J38.2, J39.2, JP19.2, JP20.2, R40.2, U10.P4, U10.P9
- new net !INT!16: J84.4, R68.1, U17.P12
- new net !INT!17: J89.4, R72.1, U18.P12
- new net !INT!18: J94.4, R76.1, U19.P12
- new net !INT!19: J99.4, R80.1, U20.P12
- new net !INT!20: J104.4, R84.1, U21.P12
- new net !INT!21: J109.4, R88.1, U22.P12
- new net !INT!22: J114.4, R92.1, U23.P12
- new net !INT!23: J119.4, R96.1, U24.P12
- new net !INT!24: J124.4, R100.1, U25.P12
- new net !INT!25: J129.4, R104.1, U26.P12
- new net !INT!26: J134.4, R108.1, U27.P12
- new net !INT!27: J139.4, R112.1, U28.P12
- new net !INT!28: J144.4, R116.1, U29.P12
- new net !INT!29: J149.4, R120.1, U30.P12
- new net GND16: C33.2, C34.2, D17.C, J81.1, J82.1, J83.1, U17.P6, U17.P7
- new net GND17: C35.2, C36.2, D18.C, J86.1, J87.1, J88.1, U18.P6, U18.P7
- new net GND18: C37.2, C38.2, D19.C, J91.1, J92.1, J93.1, U19.P6, U19.P7
- new net GND19: C39.2, C40.2, D20.C, J96.1, J97.1, J98.1, U20.P6, U20.P7
- new net GND20: C41.2, C42.2, D21.C, J101.1, J102.1, J103.1, U21.P6, U21.P7
- new net GND21: C43.2, C44.2, D22.C, J106.1, J107.1, J108.1, U22.P6, U22.P7
- new net GND22: C45.2, C46.2, D23.C, J111.1, J112.1, J113.1, U23.P6, U23.P7
- new net GND23: C47.2, C48.2, D24.C, J116.1, J117.1, J118.1, U24.P6, U24.P7
- new net GND24: C49.2, C50.2, D25.C, J121.1, J122.1, J123.1, U25.P6, U25.P7
- new net GND25: C51.2, C52.2, D26.C, J126.1, J127.1, J128.1, U26.P6, U26.P7
- new net GND26: C53.2, C54.2, D27.C, J131.1, J132.1, J133.1, U27.P6, U27.P7
- new net GND27: C55.2, C56.2, D28.C, J136.1, J137.1, J138.1, U28.P6, U28.P7
- new net GND28: C57.2, C58.2, D29.C, J141.1, J142.1, J143.1, U29.P6, U29.P7
- new net GND29: C59.2, C60.2, D30.C, J146.1, J147.1, J148.1, U30.P6, U30.P7
- new net GPI0/PWM16: J84.1, U17.P3
- new net GPI0/PWM17: J89.1, U18.P3
- new net GPI0/PWM18: J94.1, U19.P3
- new net GPI0/PWM19: J99.1, U20.P3
- new net GPI0/PWM20: J104.1, U21.P3
- new net GPI0/PWM21: J109.1, U22.P3
- new net GPI0/PWM22: J114.1, U23.P3
- new net GPI0/PWM23: J119.1, U24.P3
- new net GPI0/PWM24: J124.1, U25.P3
- new net GPI0/PWM25: J129.1, U26.P3
- new net GPI0/PWM26: J134.1, U27.P3
- new net GPI0/PWM27: J139.1, U28.P3
- new net GPI0/PWM28: J144.1, U29.P3
- new net GPI0/PWM29: J149.1, U30.P3
- new net GPI33: J84.2, U17.P2
- new net GPI34: J84.3, U17.P1
- new net GPI35: J89.2, U18.P2
- new net GPI36: J89.3, U18.P1
- new net GPI37: J94.2, U19.P2
- new net GPI38: J94.3, U19.P1
- new net GPI39: J99.2, U20.P2
- new net GPI40: J99.3, U20.P1
- new net GPI41: J104.2, U21.P2
- new net GPI42: J104.3, U21.P1
- new net GPI43: J109.2, U22.P2
- new net GPI44: J109.3, U22.P1
- new net GPI45: J114.2, U23.P2
- new net GPI46: J114.3, U23.P1
- new net GPI47: J119.2, U24.P2
- new net GPI48: J119.3, U24.P1
- new net GPI49: J124.2, U25.P2
- new net GPI50: J124.3, U25.P1
- new net GPI51: J129.2, U26.P2
- new net GPI52: J129.3, U26.P1
- new net GPI53: J134.2, U27.P2
- new net GPI54: J134.3, U27.P1
- new net GPI55: J139.2, U28.P2
- new net GPI56: J139.3, U28.P1
- new net GPI57: J144.2, U29.P2
- new net GPI58: J144.3, U29.P1
- new net GPI59: J149.2, U30.P2
- new net GPI60: J149.3, U30.P1
- new net N$100: JP66.1, R66.2
- new net N$101: M17.P$1, U17.P5
- new net N$102: M17.P$2, U17.P8
- new net N$103: D18.A, R71.1
- new net N$104: JP69.1, R71.2
- new net N$105: JP70.3, R69.2
- new net N$106: JP70.1, R70.2
- new net N$107: M18.P$1, U18.P5
- new net N$108: M18.P$2, U18.P8
- new net N$109: D19.A, R75.1
- new net N$110: JP73.1, R75.2
- new net N$111: JP74.3, R73.2
- new net N$112: JP74.1, R74.2
- new net N$113: M19.P$1, U19.P5
- new net N$114: M19.P$2, U19.P8
- new net N$115: D20.A, R79.1
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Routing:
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- added copper zone on layer 1, net GND16
- added copper zone on layer 16, net GND16
- added copper zone on layer 1, net GND17
- added copper zone on layer 16, net GND17
- added copper zone on layer 1, net GND18
- added copper zone on layer 16, net GND18
- added copper zone on layer 1, net GND19
- added copper zone on layer 16, net GND19
- added copper zone on layer 1, net GND20
- added copper zone on layer 16, net GND20
- added copper zone on layer 1, net GND21
- added copper zone on layer 16, net GND21
- added copper zone on layer 1, net GND22
- added copper zone on layer 16, net GND22
- added copper zone on layer 1, net GND23
- added copper zone on layer 16, net GND23
- added copper zone on layer 1, net GND24
- added copper zone on layer 16, net GND24
- added copper zone on layer 1, net GND25
- added copper zone on layer 16, net GND25
- added copper zone on layer 1, net GND26
- added copper zone on layer 16, net GND26
- added copper zone on layer 1, net GND27
- added copper zone on layer 16, net GND27
- added copper zone on layer 1, net GND28
- added copper zone on layer 16, net GND28
- added copper zone on layer 1, net GND29
- added copper zone on layer 16, net GND29
- added copper zone on layer 1, net VDD
- added copper zone on layer 1, net VDD1
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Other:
- board size 123.2 x 117.3 mm -> 149.1 x 192 mm
- board text added: "v10"
- board text removed: "v01"
